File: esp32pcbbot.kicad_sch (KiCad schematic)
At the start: 44 parts, among them IC1 BMI055, J1 TB002-500-02BE, J2 TB002-500-02BE, J3 TB002-500-02BE, J4 215299-4, J5 SSQ-120-01-L-D, J6 215299-4, Q1 2N7002, Q2 2N7002, Q3 Q_Photo_NPN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

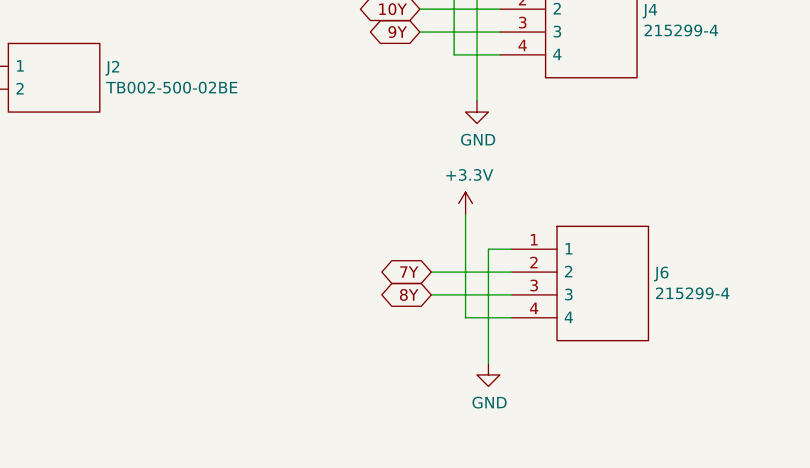
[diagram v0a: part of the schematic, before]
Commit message: fixed i2c breakout, updated TODO
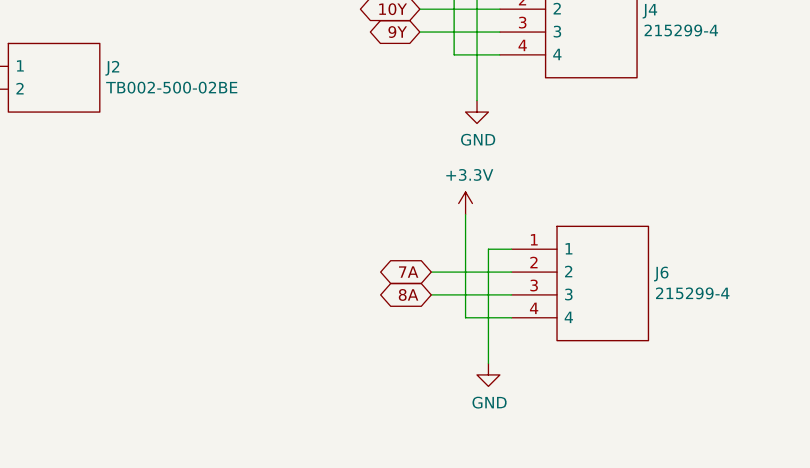
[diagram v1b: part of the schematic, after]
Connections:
- net 7A: now also J6.2
- net 7Y: no longer J6.2
- net 8A: now also J6.3
- net 8Y: no longer J6.3
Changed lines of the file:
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@@
     )
   )
-  (global_label "7Y" (shape bidirectional) (at 86.36 262.89 180) (fields_autoplaced)
+  (global_label "7A" (shape bidirectional) (at 86.36 262.89 180) (fields_autoplaced)
     (effects (font (size 1.27 1.27)) (justify right))
-    (property "Intersheet References" "${INTERSHEET_REFS}" (id 0) (at 0 0 0)
-      (effects (font (size 1.27 1.27)) hide)
+    (property "Intersheet References" "${INTERSHEET_REFS}" (id 0) (at 81.7377 262.8106 0)
+      (effects (font (size 1.27 1.27)) (justify right) hide)
     )
   )
@@
     )
   )
-  (global_label "8Y" (shape bidirectional) (at 86.36 265.43 180) (fields_autoplaced)
+  (global_label "8A" (shape bidirectional) (at 86.36 265.43 180) (fields_autoplaced)
     (effects (font (size 1.27 1.27)) (justify right))
-    (property "Intersheet References" "${INTERSHEET_REFS}" (id 0) (at 0 0 0)
-      (effects (font (size 1.27 1.27)) hide)
+    (property "Intersheet References" "${INTERSHEET_REFS}" (id 0) (at 81.7377 265.3506 0)
+      (effects (font (size 1.27 1.27)) (justify right) hide)
     )
   )

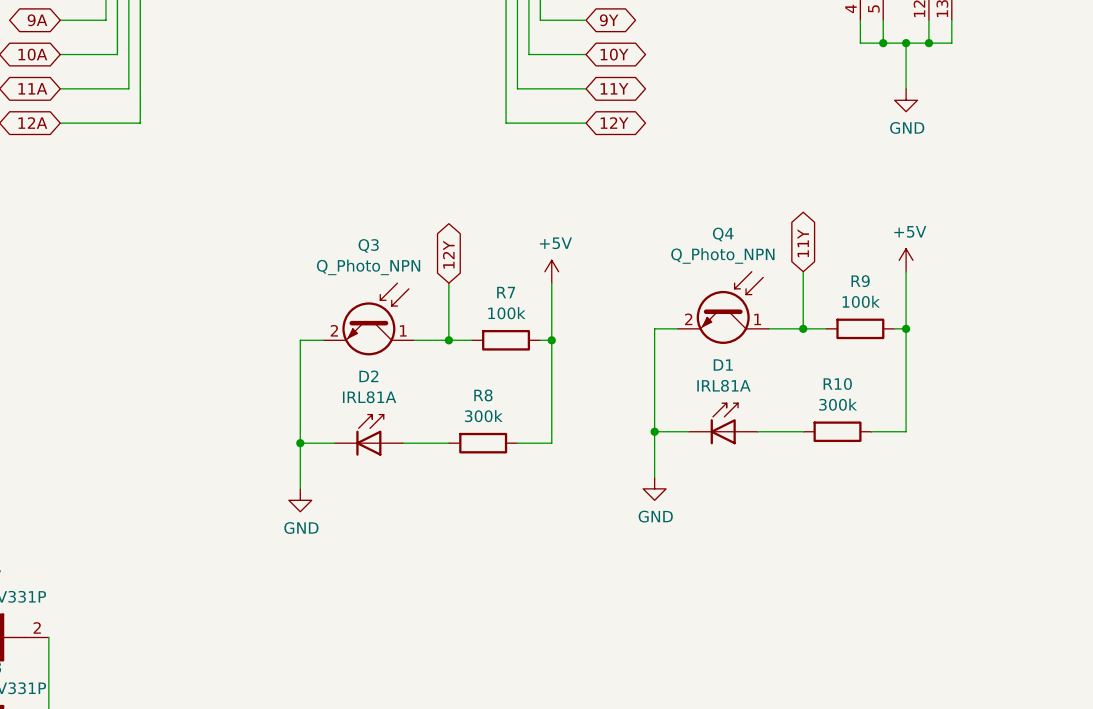
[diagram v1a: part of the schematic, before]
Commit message: updated IR sensors
Switched to an easier to use IR reflectivity module
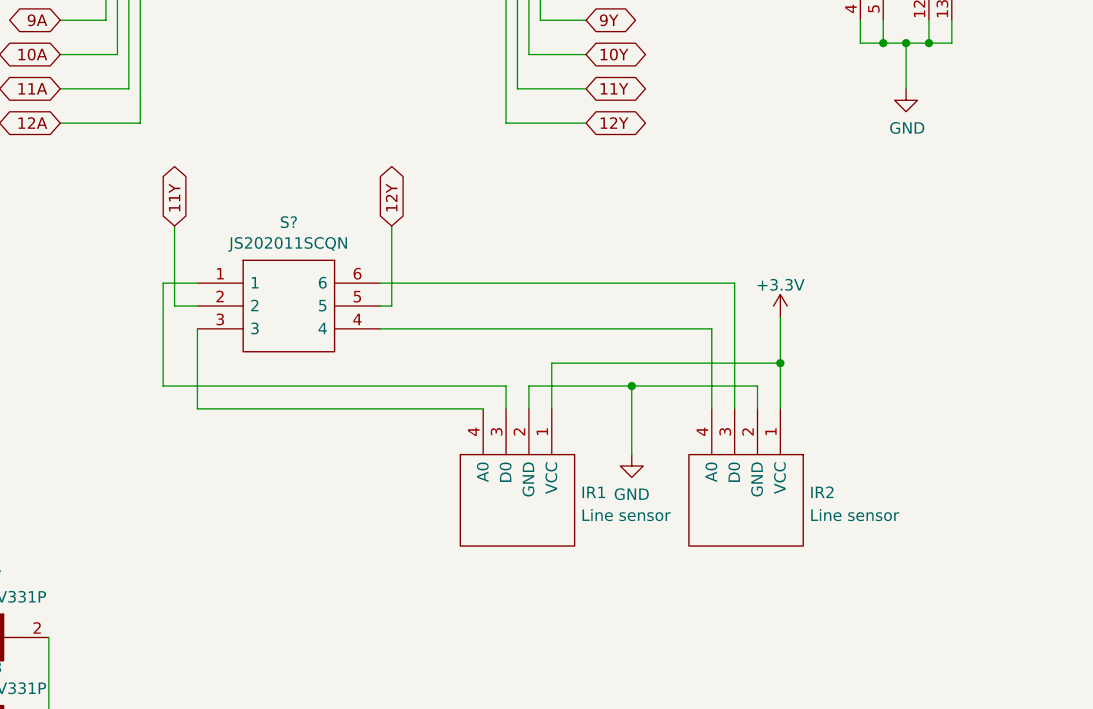
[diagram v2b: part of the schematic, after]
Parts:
- removed D1, D2: IRL81A, LED_THT:LED_D3.0mm, symbol LED:IRL81A
- removed Q3, Q4: Q_Photo_NPN, SamacSys_Parts:QSD124A4R0, symbol Device:Q_Photo_NPN
- removed R10, R8: 300k, Resistor_SMD:R_0603_1608Metric, symbol Device:R
- removed R7, R9: 100k, Resistor_SMD:R_0603_1608Metric, symbol Device:R
- added IR1, IR2: Line sensor, custom_components:IR reflectivity sensor, symbol esp32pcbbot-rescue:Line sensor
- added S?: JS202011SCQN, JS202011SCQN, symbol SamacSys_Parts:JS202011SCQN
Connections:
- net +3V3: now also IR1.1 (VCC), IR2.1 (VCC)
- net 11Y: now also S?.2
- net 12Y: now also S?.5
- net GND: now also IR1.2 (GND), IR2.2 (GND)
- new net: IR1.3 (D0), S?.1
- new net: IR1.4 (A0), S?.3
- new net: IR2.4 (A0), S?.4
- new net: IR2.3 (D0), S?.6
